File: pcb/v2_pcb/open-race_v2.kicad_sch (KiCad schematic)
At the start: 0 parts

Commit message: start pcb v2
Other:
- added sheet HexaSPI_PSRAM (HexaSPI_PSRAM.kicad_sch)
- sheet STM32_MCU_IO: file untitled.kicad_sch -> STM32_MCU_IO.kicad_sch
- sheet STM32_MCU_PWR ports: added MCUPower; removed none
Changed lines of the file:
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@@
 			)
 		)
-		(property "Sheetfile" "untitled.kicad_sch"
+		(property "Sheetfile" "STM32_MCU_IO.kicad_sch"
 			(at 116.84 179.6546 0)
 			(show_name no)
@@
 	)
 	(sheet
-		(at 39.37 24.13)
+		(at 55.88 46.99)
+		(size 43.18 10.16)
+		(exclude_from_sim no)
+		(in_bom yes)
+		(on_board yes)
+		(dnp no)
+		(fields_autoplaced yes)
+		(stroke
+			(width 0.1524)
+			(type solid)
+		)
+		(fill
+			(color 0 0 0 0)
+		)
+		(property "Sheetname" "HexaSPI_PSRAM"
+			(at 55.88 46.2784 0)
+			(show_name no)
+			(do_not_autoplace no)
+			(effects
+				(font
+					(size 1.27 1.27)
+				)
+				(justify left bottom)
+			)
+		)
+		(property "Sheetfile" "HexaSPI_PSRAM.kicad_sch"
+			(at 55.88 57.7346 0)
+			(show_name no)
+			(do_not_autoplace no)
+			(effects
+				(font
+					(size 1.27 1.27)
+				)
+				(justify left top)
+			)
+		)
+		(instances
+			(project "open-race_v2"
+				(path "/1cc14db4-4207-4c76-b5f6-6a2491c5fa6b"
+					(page "4")
+				)
+			)
+		)
+	)
+	(sheet
+		(at 55.88 24.13)
 		(size 43.18 10.16)
 		(exclude_from_sim no)
@@
 		)
 		(property "Sheetname" "STM32_MCU_PWR"
-			(at 39.37 23.4184 0)
+			(at 55.88 23.4184 0)
 			(show_name no)
 			(do_not_autoplace no)
@@
 		)
 		(property "Sheetfile" "stm32power.kicad_sch"
-			(at 39.37 34.8746 0)
+			(at 55.88 34.8746 0)
 			(show_name no)
 			(do_not_autoplace no)
@@
 			)
 		)
+		(pin "MCUPower" input
+			(at 99.06 30.48 0)
+			(effects
+				(font
+					(size 1.27 1.27)
+				)
+				(justify right)
+			)
+		)

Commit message: contineu pcb
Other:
- added sheet OctoSPI_FLASH (OctoSPI_FLASH.kicad_sch)
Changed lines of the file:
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@@
+	)
+	(sheet
+		(at 55.88 64.77)
+		(size 43.18 10.16)
+		(exclude_from_sim no)
+		(in_bom yes)
+		(on_board yes)
+		(dnp no)
+		(fields_autoplaced yes)
+		(stroke
+			(width 0.1524)
+			(type solid)
+		)
+		(fill
+			(color 0 0 0 0)
+		)
+		(property "Sheetname" "OctoSPI_FLASH"
+			(at 55.88 64.0584 0)
+			(show_name no)
+			(do_not_autoplace no)
+			(effects
+				(font
+					(size 1.27 1.27)
+				)
+				(justify left bottom)
+			)
+		)
+		(property "Sheetfile" "OctoSPI_FLASH.kicad_sch"
+			(at 55.88 75.5146 0)
+			(show_name no)
+			(do_not_autoplace no)
+			(effects
+				(font
+					(size 1.27 1.27)
+				)
+				(justify left top)
+			)
+		)
+		(instances
+			(project "open-race_v2"
+				(path "/1cc14db4-4207-4c76-b5f6-6a2491c5fa6b"
+					(page "5")
+				)
+			)
+		)
 	)
 	(sheet

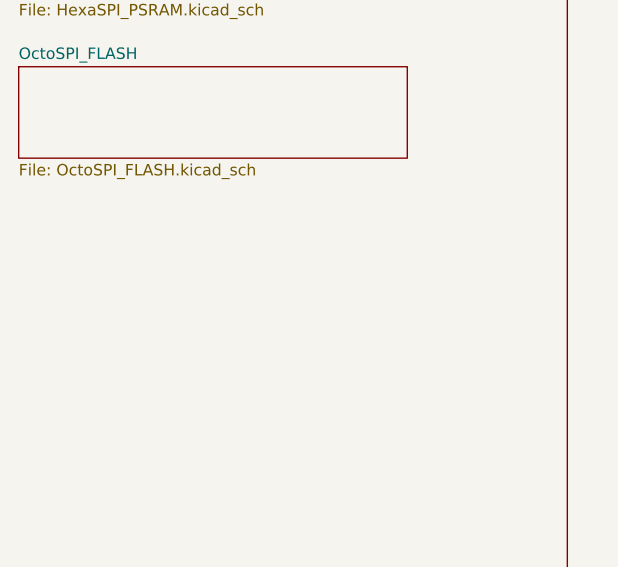
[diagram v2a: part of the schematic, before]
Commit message: add debug to pcb
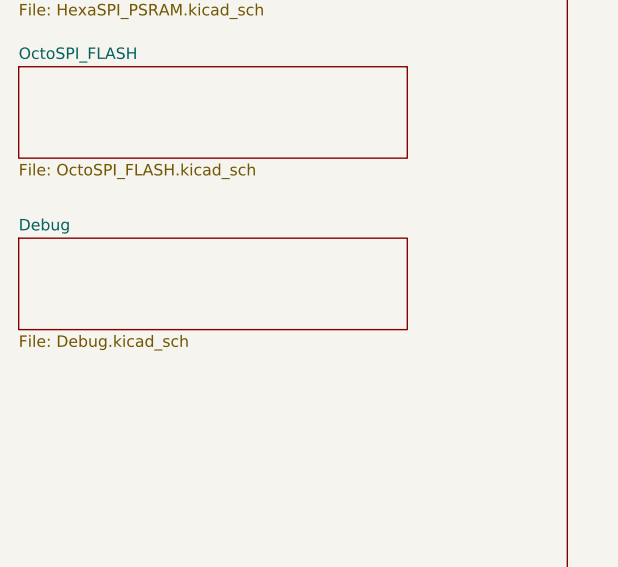
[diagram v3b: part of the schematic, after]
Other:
- added sheet Debug (Debug.kicad_sch)
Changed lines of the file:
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@@
 	(paper "A4")
+	(sheet
+		(at 55.88 83.82)
+		(size 43.18 10.16)
+		(exclude_from_sim no)
+		(in_bom yes)
+		(on_board yes)
+		(dnp no)
+		(fields_autoplaced yes)
+		(stroke
+			(width 0.1524)
+			(type solid)
+		)
+		(fill
+			(color 0 0 0 0)
+		)
+		(property "Sheetname" "Debug"
+			(at 55.88 83.1084 0)
+			(show_name no)
+			(do_not_autoplace no)
+			(effects
+				(font
+					(size 1.27 1.27)
+				)
+				(justify left bottom)
+			)
+		)
+		(property "Sheetfile" "Debug.kicad_sch"
+			(at 55.88 94.5646 0)
+			(show_name no)
+			(do_not_autoplace no)
+			(effects
+				(font
+					(size 1.27 1.27)
+				)
+				(justify left top)
+			)
+		)
+		(instances
+			(project "open-race_v2"
+				(path "/1cc14db4-4207-4c76-b5f6-6a2491c5fa6b"
+					(page "6")
+				)
+			)
+		)
+	)
 	(sheet
 		(at 116.84 17.78)

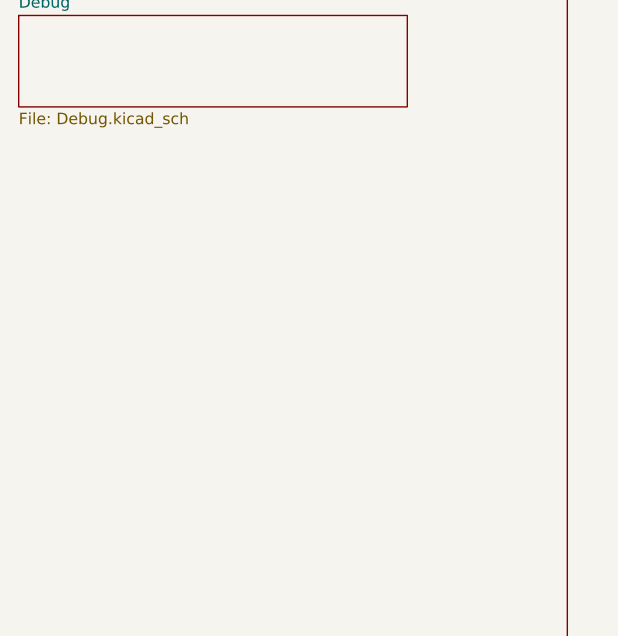
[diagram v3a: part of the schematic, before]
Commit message: add usb to schematic
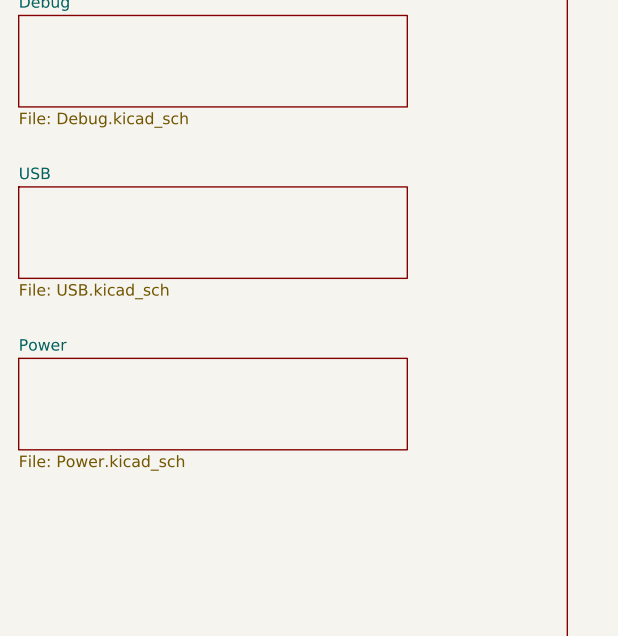
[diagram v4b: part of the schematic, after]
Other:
- added sheet Power (Power.kicad_sch)
- added sheet USB (USB.kicad_sch)
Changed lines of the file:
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@@
+	)
+	(sheet
+		(at 55.88 102.87)
+		(size 43.18 10.16)
+		(exclude_from_sim no)
+		(in_bom yes)
+		(on_board yes)
+		(dnp no)
+		(fields_autoplaced yes)
+		(stroke
+			(width 0.1524)
+			(type solid)
+		)
+		(fill
+			(color 0 0 0 0)
+		)
+		(property "Sheetname" "USB"
+			(at 55.88 102.1584 0)
+			(show_name no)
+			(do_not_autoplace no)
+			(effects
+				(font
+					(size 1.27 1.27)
+				)
+				(justify left bottom)
+			)
+		)
+		(property "Sheetfile" "USB.kicad_sch"
+			(at 55.88 113.6146 0)
+			(show_name no)
+			(do_not_autoplace no)
+			(effects
+				(font
+					(size 1.27 1.27)
+				)
+				(justify left top)
+			)
+		)
+		(instances
+			(project "open-race_v2"
+				(path "/1cc14db4-4207-4c76-b5f6-6a2491c5fa6b"
+					(page "7")
+				)
+			)
+		)
 	)
 	(sheet
@@
 				)
 			)
+		)
+	)
+	(sheet
+		(at 55.88 121.92)
+		(size 43.18 10.16)
+		(exclude_from_sim no)
+		(in_bom yes)
+		(on_board yes)
+		(dnp no)
+		(fields_autoplaced yes)
+		(stroke
+			(width 0.1524)
+			(type solid)
+		)
+		(fill
+			(color 0 0 0 0)
+		)
+		(property "Sheetname" "Power"
+			(at 55.88 121.2084 0)
+			(show_name no)
+			(do_not_autoplace no)
+			(effects
+				(font
+					(size 1.27 1.27)
+				)
+				(justify left bottom)
+			)
+		)
+		(property "Sheetfile" "Power.kicad_sch"
+			(at 55.88 132.6646 0)
+			(show_name no)
+			(do_not_autoplace no)
+			(effects
+				(font
+					(size 1.27 1.27)
+				)
+				(justify left top)
+			)
+		)
+		(instances
+			(project "open-race_v2"
+				(path "/1cc14db4-4207-4c76-b5f6-6a2491c5fa6b"
+					(page "8")
+				)
+			)
